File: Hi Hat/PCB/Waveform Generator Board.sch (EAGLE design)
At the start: 94 parts, among them IC1 LM741P, Q1 2N2222A, Q10 2N3904, Q11 2N3904, Q12 2N3904, Q2 2N2222A, Q3 2N2222A, Q4 2N2222A, Q5 2N2222A, Q6 2N2222A, Q7 2N2222A, Q8 2N2222A, Q9 2N3904

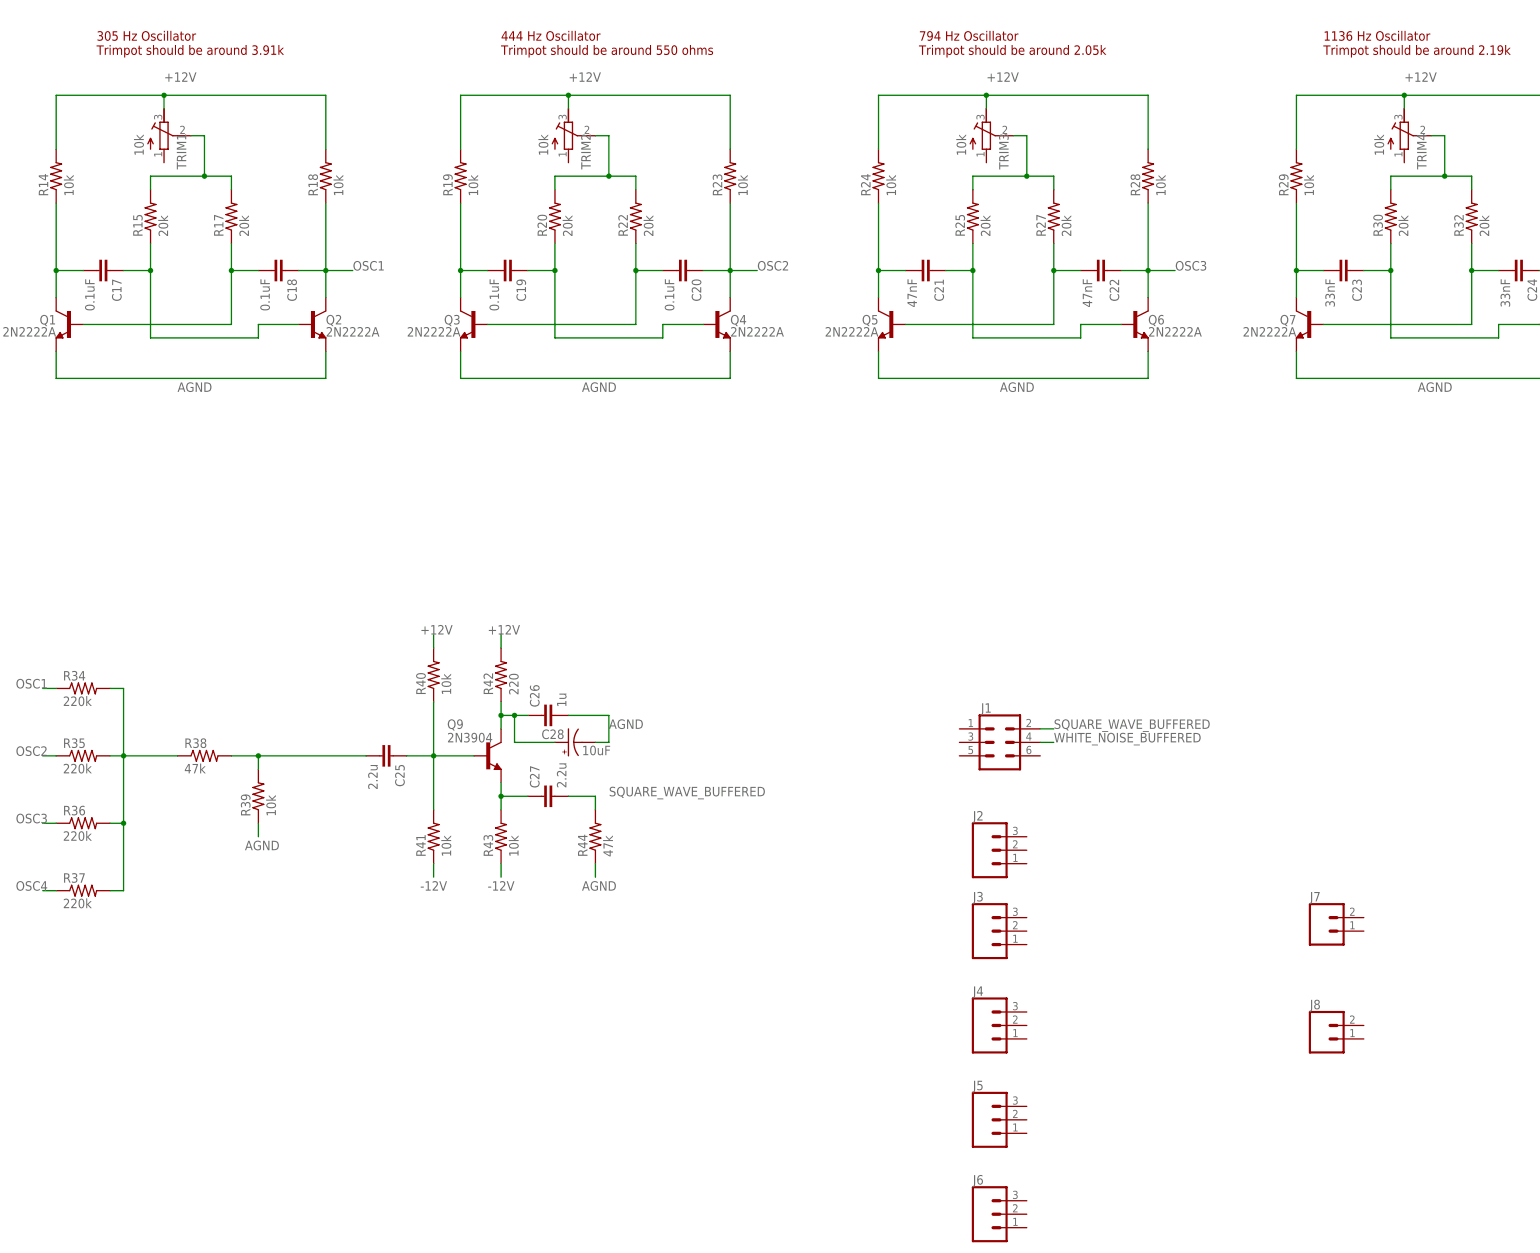
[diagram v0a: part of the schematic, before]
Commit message: Worked on Hi-hat and waveform generator board
Changed trimpots to the proper part. Added test points to the waveform generator board and fixed silkscreen, ran DRC.
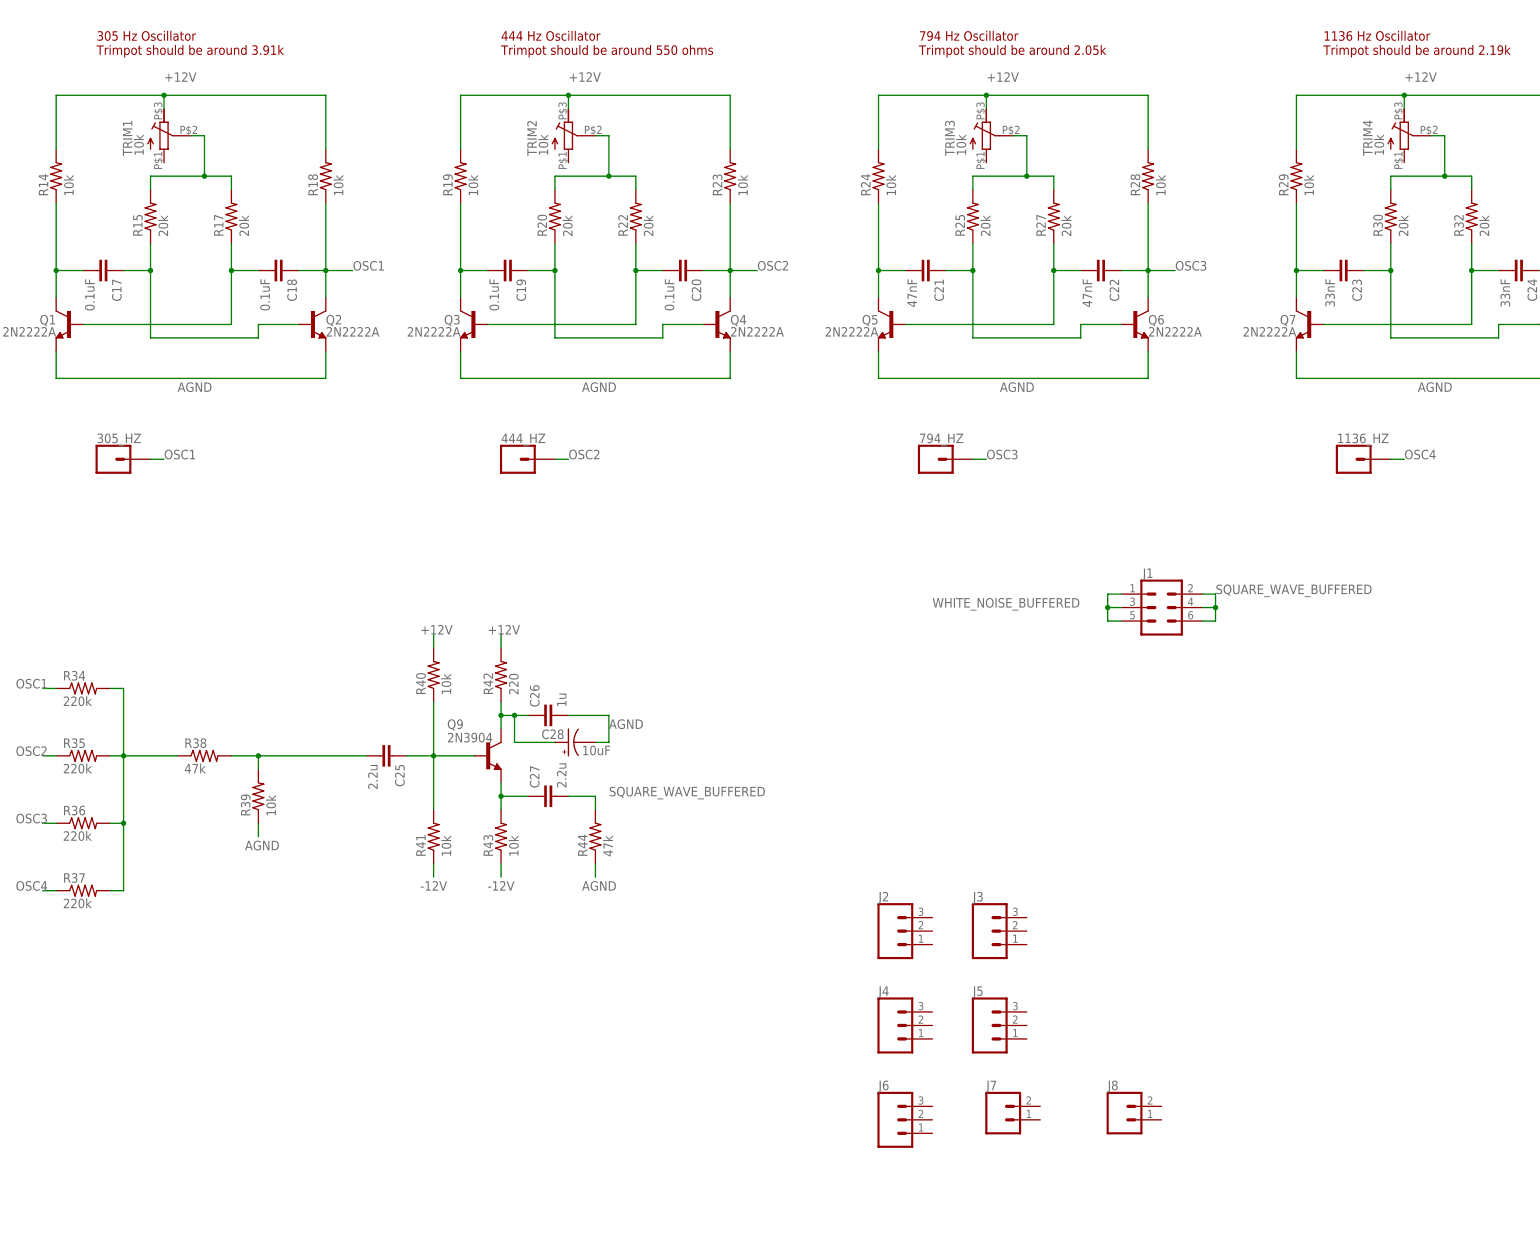
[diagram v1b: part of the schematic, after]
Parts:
- added 1136_HZ, 305_HZ, 444_HZ, 794_HZ: (no value), SparkFun-Connectors:CONN_01PTH_NO_SILK_KIT
- TRIM1, TRIM2, TRIM3, TRIM4: device rcl:R-TRIMM64W -> Capstone:10K_TRIMMER
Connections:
- net OSC1: now also 305_HZ.1
- net OSC2: now also 444_HZ.1
- net OSC3: now also 794_HZ.1
- net OSC4: now also 1136_HZ.1
- net SQUARE_WAVE_BUFFERED: now also J1.4, J1.6
- net WHITE_NOISE_BUFFERED: now also J1.1, J1.3, J1.5; no longer J1.4
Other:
- moved on the sheet: J1, J2, J4, J5, J6, J7, J8, TRIM1, TRIM2, TRIM3, TRIM4

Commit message: Cleaned up schematics
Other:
- note added: "24 Pin Header"
- note added: "Output to Cymbals"
- note added: "Square Wave Buffer"
- note added: "Square Wave Generators"
- moved on the sheet: 1136_HZ, 305_HZ, 444_HZ, 794_HZ, C17, C18, C19, C20, C21, C22, C23, C24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
